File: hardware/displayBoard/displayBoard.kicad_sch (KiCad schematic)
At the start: 33 parts, among them J1 Conn_01x10_Pin, Q1 MMBTA42, Q10 MMBTA42, Q11 BSS123, Q2 MMBTA42, Q3 MMBTA42, Q4 MMBTA42, Q5 MMBTA42, Q6 MMBTA42, Q7 MMBTA42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

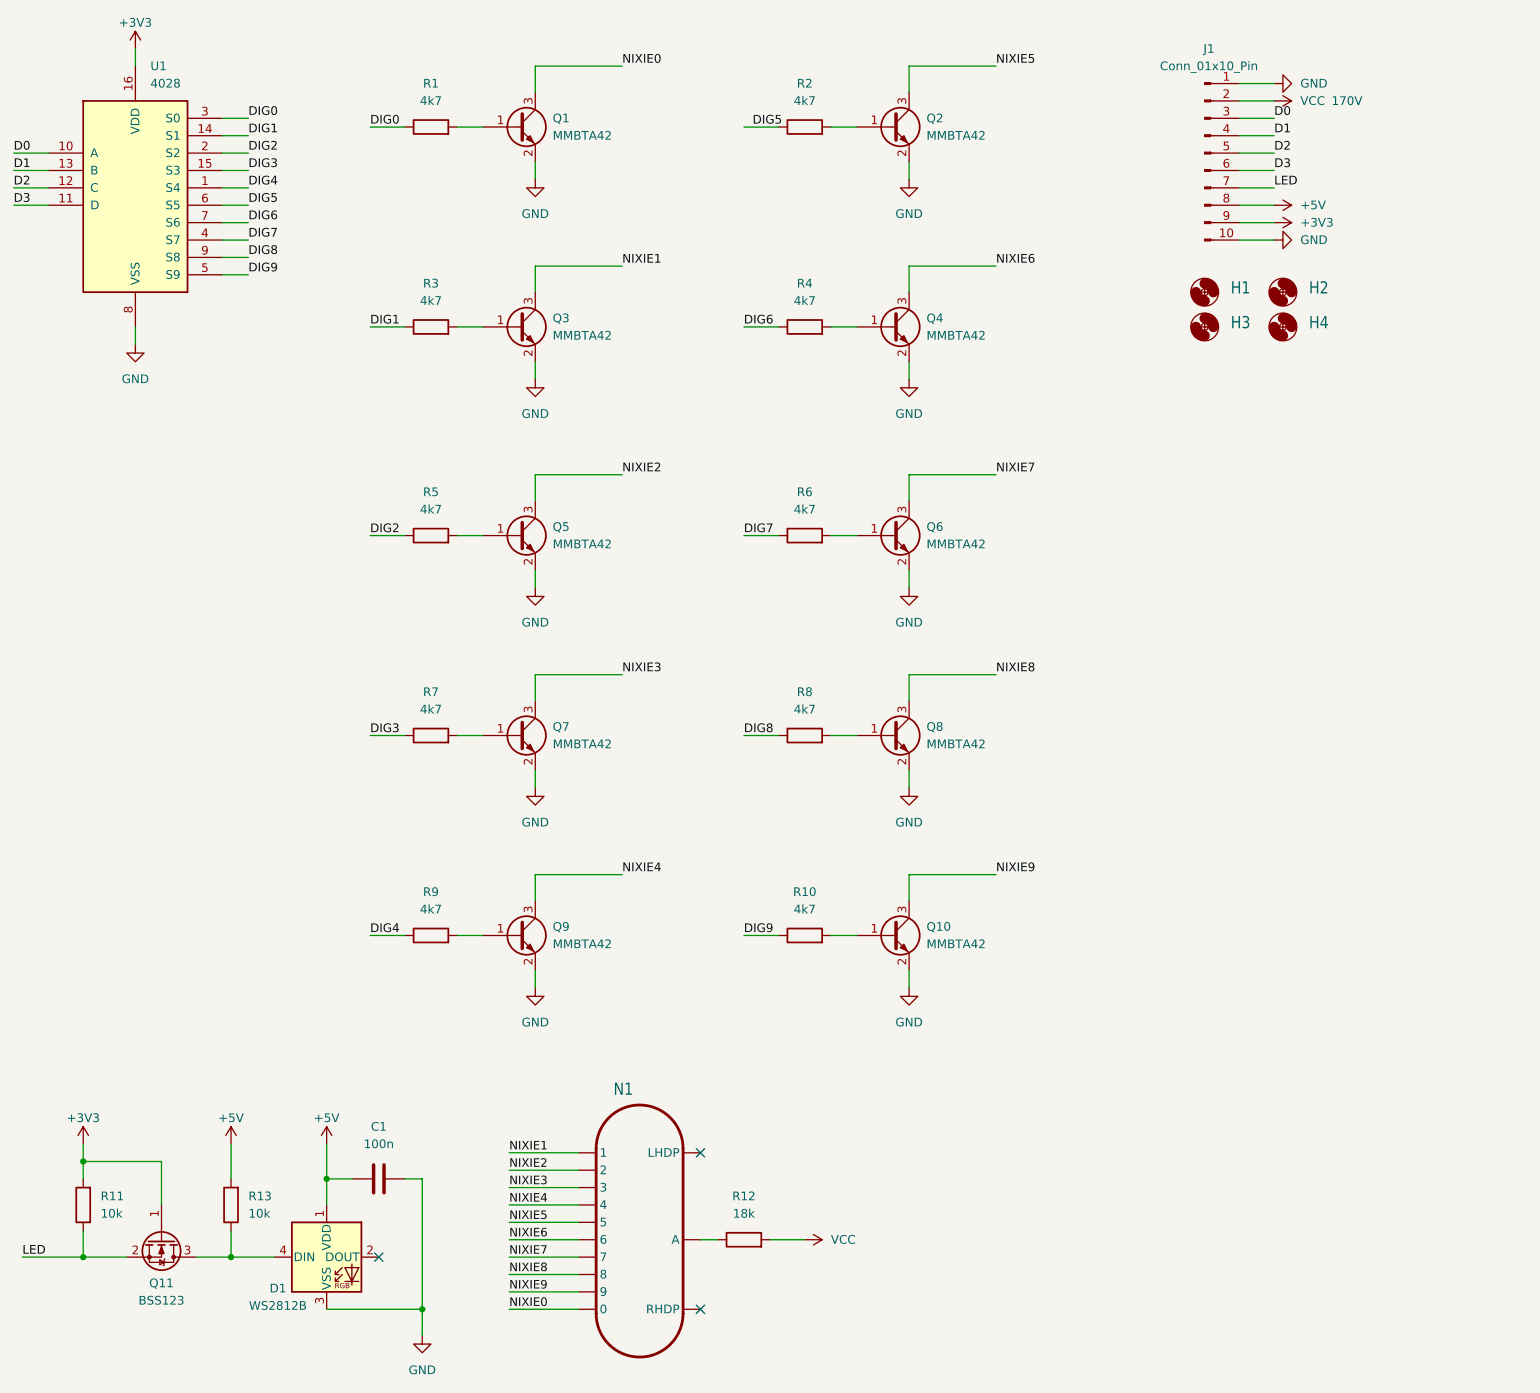
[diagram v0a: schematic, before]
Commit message: Add pull-ups to BCD decoder inputs
- Add pull-up resistors to BCD decoder to prevent turning on the nixie tube during boot
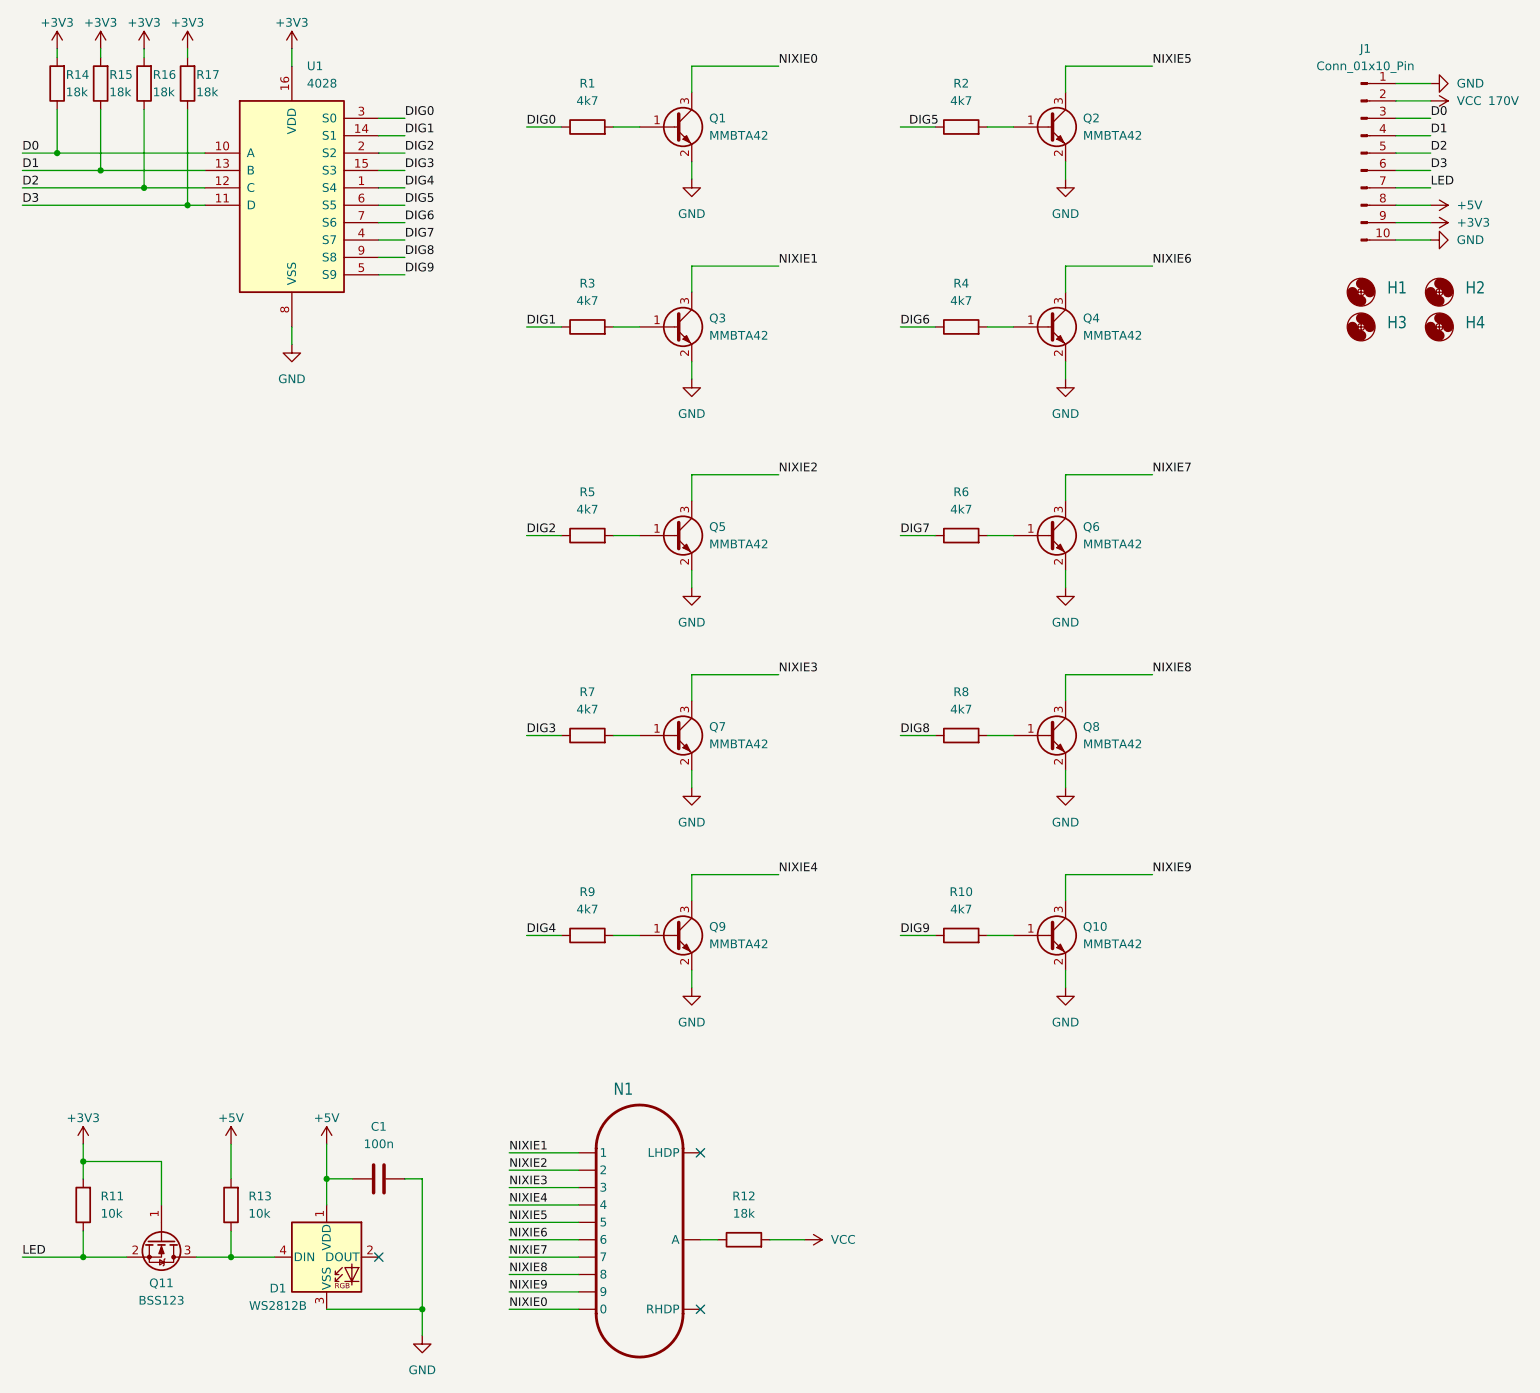
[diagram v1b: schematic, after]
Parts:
- added R14, R15, R16, R17: 18k, Resistor_SMD:R_0603_1608Metric, symbol Device:R
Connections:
- net +3V3: now also R14.2, R15.2, R16.2, R17.2
- net D0: now also R14.1
- net D1: now also R15.1
- net D2: now also R16.1
- net D3: now also R17.1
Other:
- moved on the sheet: H1, H2, H3, H4, J1, Q1, Q10, Q2, Q3, Q4, Q5, Q6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

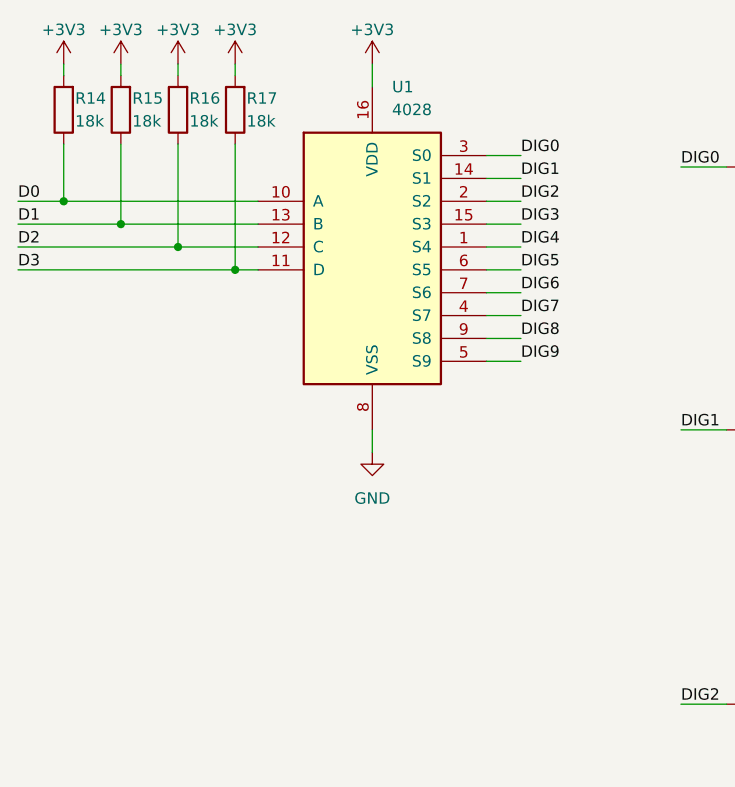
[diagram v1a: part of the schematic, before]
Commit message: Add a decoupling cap to CD4028
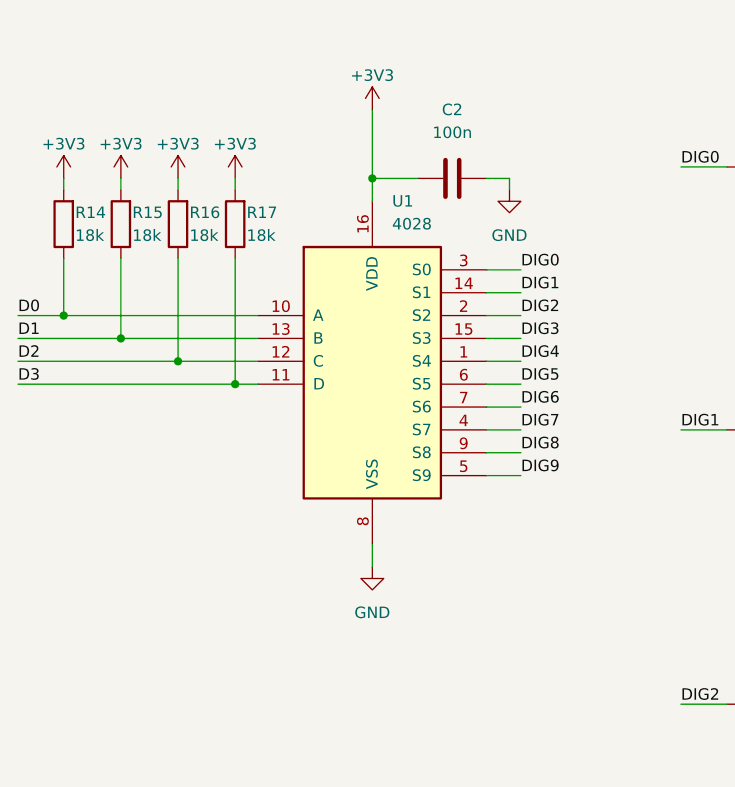
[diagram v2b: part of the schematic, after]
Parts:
- added C2: 100n, Capacitor_SMD:C_0603_1608Metric, symbol Device:C
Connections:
- net +3V3: now also C2.1
- net GND: now also C2.2
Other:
- moved on the sheet: R14, R15, R16, R17, U1
